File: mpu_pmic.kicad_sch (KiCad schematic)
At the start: 56 parts, among them J501 36103505, U501 STPMIC1DPQR

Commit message: Clean-up schematics
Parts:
- L501, L502, L503, L504: MPN (none) -> DFE252012P-1R0M=P2
- R504, R505, R506, R507, R508, R509: value 33 Ω -> 0 Ω
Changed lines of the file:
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@@
 			)
 		)
-		(property "MPN" ""
+		(property "MPN" "DFE252012P-1R0M=P2"
 			(at 208.28 129.54 90)
 			(effects
@@
 			)
 		)
-		(property "Value" "33 Ω"
+		(property "Value" "0 Ω"
 			(at 155.448 202.692 90)
 			(effects
@@
 			)
 		)
-		(property "MPN" ""
+		(property "MPN" "DFE252012P-1R0M=P2"
 			(at 208.28 137.16 90)
 			(effects
@@
 			)
 		)
-		(property "Value" "33 Ω"
+		(property "Value" "0 Ω"
 			(at 155.448 195.072 90)
 			(effects
@@
 			)
 		)
-		(property "Value" "33 Ω"
+		(property "Value" "0 Ω"
 			(at 155.448 200.152 90)
 			(effects
@@
 			)
 		)
-		(property "Value" "33 Ω"
+		(property "Value" "0 Ω"
 			(at 155.448 197.612 90)
 			(effects
@@
 			)
 		)
-		(property "Value" "33 Ω"
+		(property "Value" "0 Ω"
 			(at 155.448 192.532 90)
 			(effects
@@
 			)
 		)
-		(property "MPN" ""
+		(property "MPN" "DFE252012P-1R0M=P2"
 			(at 208.28 114.3 90)
 			(effects
@@
 			)
 		)
-		(property "MPN" ""
+		(property "MPN" "DFE252012P-1R0M=P2"
 			(at 208.28 121.92 90)
 			(effects
@@
 			)
 		)
-		(property "Value" "33 Ω"
+		(property "Value" "0 Ω"
 			(at 203.2 191.516 90)
 			(effects

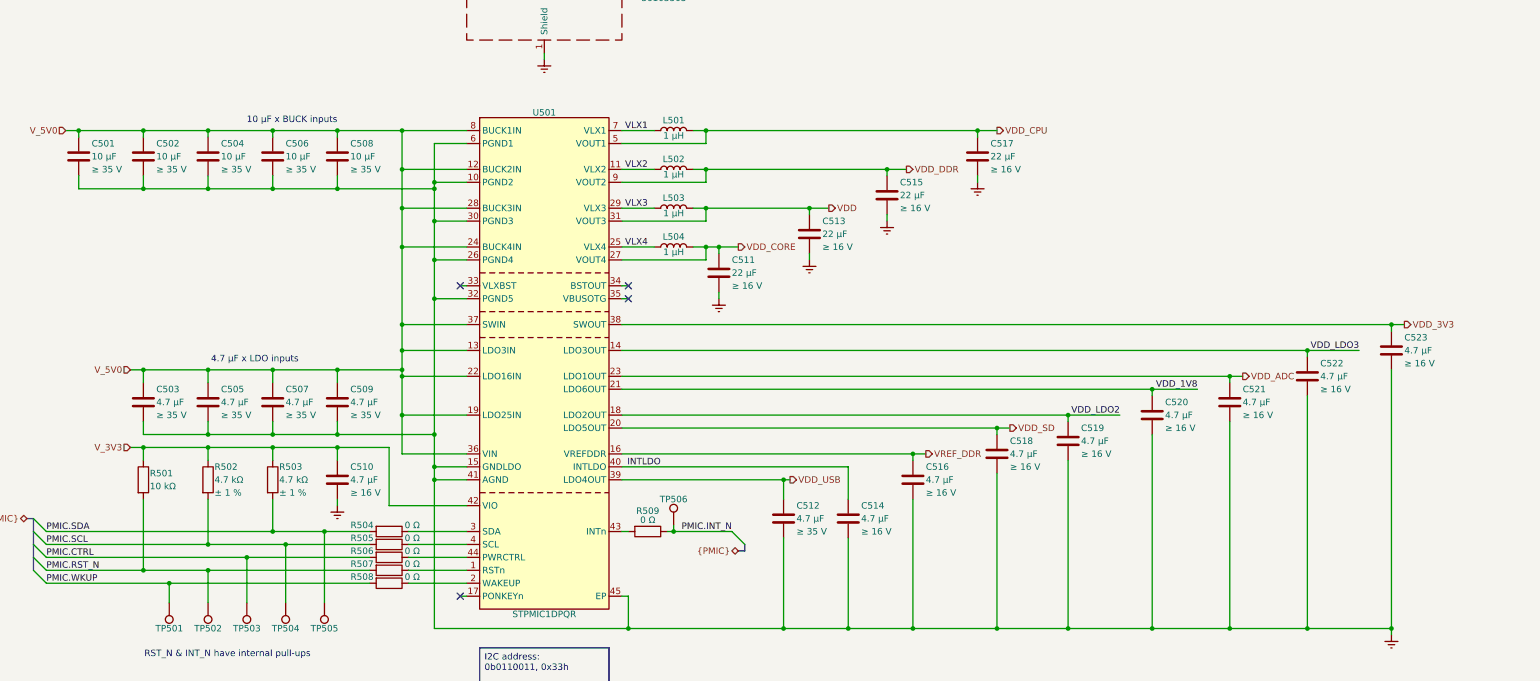
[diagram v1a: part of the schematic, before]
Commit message: Add additional info to passives
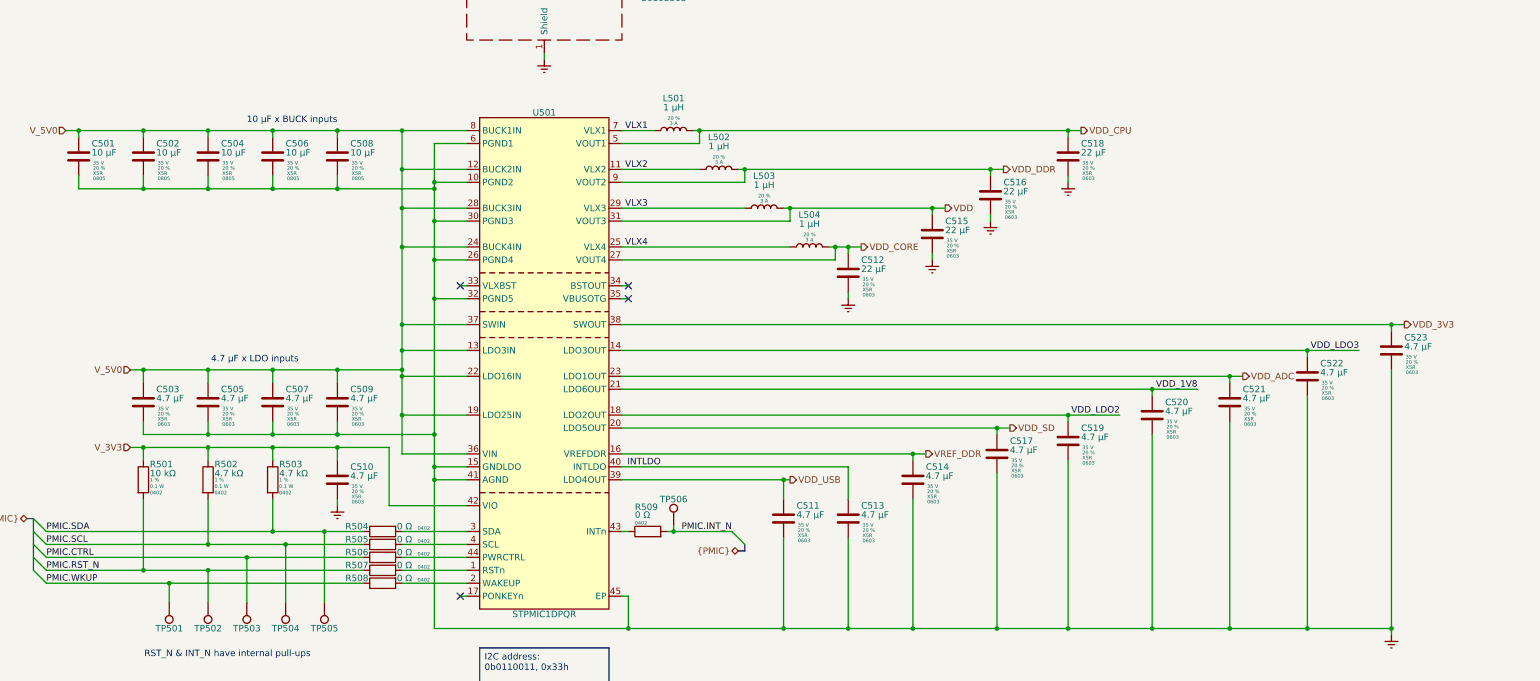
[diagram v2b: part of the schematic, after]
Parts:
- C501, C502, C504, C506, C508: footprint Capacitor_SMD:C_0603_1608Metric -> (none); MPN GRM188R6YA106MA73D -> (none); Manufacturer Murata Electronics -> (none); Size (none) -> 0805; Temperature coefficient (none) -> X5R; Tolerance (none) -> 20 %; Voltage rating ≥ 35 V -> 35 V
- C503, C505, C507, C509: footprint Capacitor_SMD:C_0603_1608Metric -> (none); MPN GRM188R6YA475KE15D -> (none); Manufacturer Murata Electronics -> (none); Size (none) -> 0603; Temperature coefficient (none) -> X5R; Tolerance (none) -> 20 %; Voltage rating ≥ 35 V -> 35 V
- C510, C514, C519, C520, C521, C522, C523: footprint Capacitor_SMD:C_0603_1608Metric -> (none); MPN GRM188R6YA475KE15D -> (none); Manufacturer Murata Electronics -> (none); Size (none) -> 0603; Temperature coefficient (none) -> X5R; Tolerance (none) -> 20 %; Voltage rating ≥ 16 V -> 35 V
- C511, C513, C517: value 22 µF -> 4.7 µF; footprint Capacitor_SMD:C_0603_1608Metric -> (none); MPN GRM188R6YA106MA73D -> (none); Manufacturer Murata Electronics -> (none); Size (none) -> 0603; Temperature coefficient (none) -> X5R; Tolerance (none) -> 20 %; Voltage rating ≥ 16 V -> 35 V
- C512: value 4.7 µF -> 22 µF; footprint Capacitor_SMD:C_0603_1608Metric -> (none); MPN GRM188R6YA475KE15D -> (none); Manufacturer Murata Electronics -> (none); Size (none) -> 0603; Temperature coefficient (none) -> X5R; Tolerance (none) -> 20 %; Voltage rating ≥ 35 V -> 35 V
- C515: footprint Capacitor_SMD:C_0603_1608Metric -> (none); MPN GRM188R6YA106MA73D -> (none); Manufacturer Murata Electronics -> (none); Size (none) -> 0603; Temperature coefficient (none) -> X5R; Tolerance (none) -> 20 %; Voltage rating ≥ 16 V -> 35 V
- C516, C518: value 4.7 µF -> 22 µF; footprint Capacitor_SMD:C_0603_1608Metric -> (none); MPN GRM188R6YA475KE15D -> (none); Manufacturer Murata Electronics -> (none); Size (none) -> 0603; Temperature coefficient (none) -> X5R; Tolerance (none) -> 20 %; Voltage rating ≥ 16 V -> 35 V
- L501, L502, L503, L504: footprint (none) -> Inductor_SMD:L_1008_2520Metric; Current rating (none) -> 3 A; Digi-Key Part Number (none) -> 490-10647-1-ND; Manufacturer (none) -> Murata Electronics; Tolerance (none) -> 20 %
- R501: MPN 560112110020 -> (none); Manufacturer Würth Elektronik -> (none); Power rating (none) -> 0.1 W; Size (none) -> 0402; Tolerance (none) -> 1 %
- R502, R503: Power rating (none) -> 0.1 W; Size (none) -> 0402; Tolerance ± 1 % -> 1 %
- R504, R505, R506, R507, R508, R509: footprint perfect_footprints:R_0402_1005Metric -> (none); MPN 560112110020 -> (none); Manufacturer Würth Elektronik -> (none); Size (none) -> 0402
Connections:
- net INTLDO: now also C513.1; no longer C514.1
- net PMIC.CTRL: now also R506.1; no longer R506.2
- net PMIC.INT_N: now also R509.2; no longer R509.1
- net PMIC.RST_N: now also R507.1; no longer R507.2
- net PMIC.SCL: now also R505.1; no longer R505.2
- net PMIC.SDA: now also R504.1; no longer R504.2
- net PMIC.WKUP: now also R508.1; no longer R508.2
- net VDD: now also C515.1; no longer C513.1
- net VDD_CORE: now also C512.1; no longer C511.1
- net VDD_CPU: now also C518.1; no longer C517.1
- net VDD_DDR: now also C516.1; no longer C515.1
- net VDD_SD: now also C517.1; no longer C518.1
- net VDD_USB: now also C511.1; no longer C512.1
- net VREF_DDR: now also C514.1; no longer C516.1
- net at U501.1 (RSTn): now also R507.2; no longer R507.1
- net at U501.2 (WAKEUP): now also R508.2; no longer R508.1
- net at U501.3 (SDA): now also R504.2; no longer R504.1
- net at U501.4 (SCL): now also R505.2; no longer R505.1
- net at U501.43 (INTn): now also R509.1; no longer R509.2
- net at U501.44 (PWRCTRL): now also R506.2; no longer R506.1

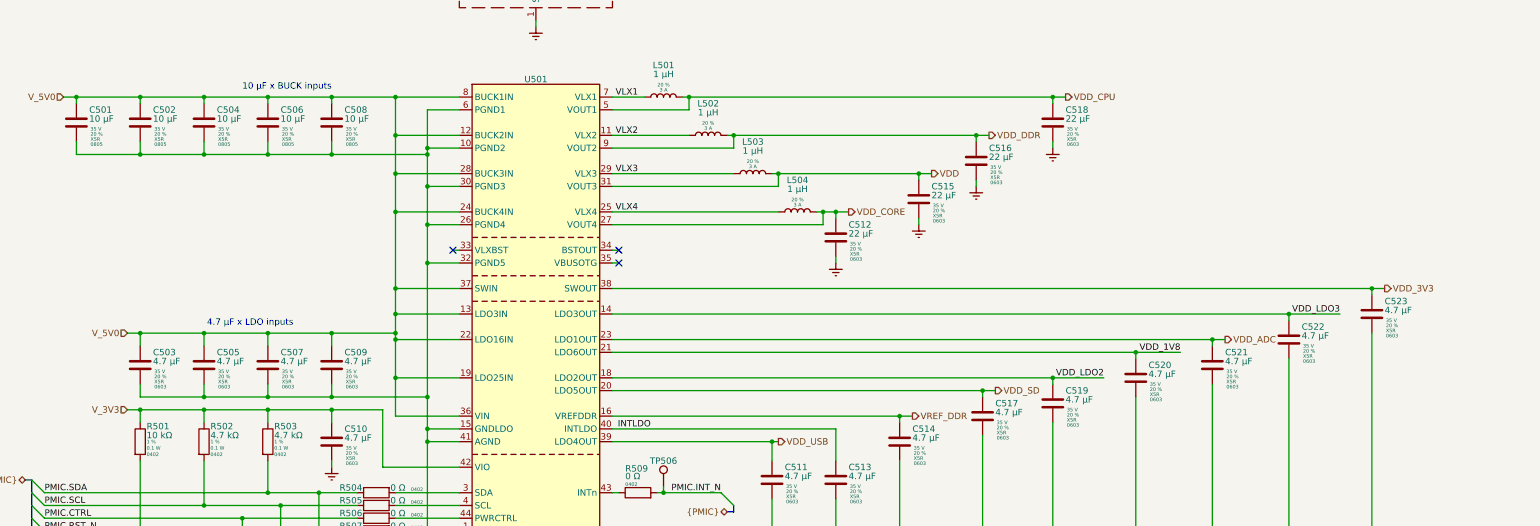
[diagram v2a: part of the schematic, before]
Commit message: Update capacitor BOM
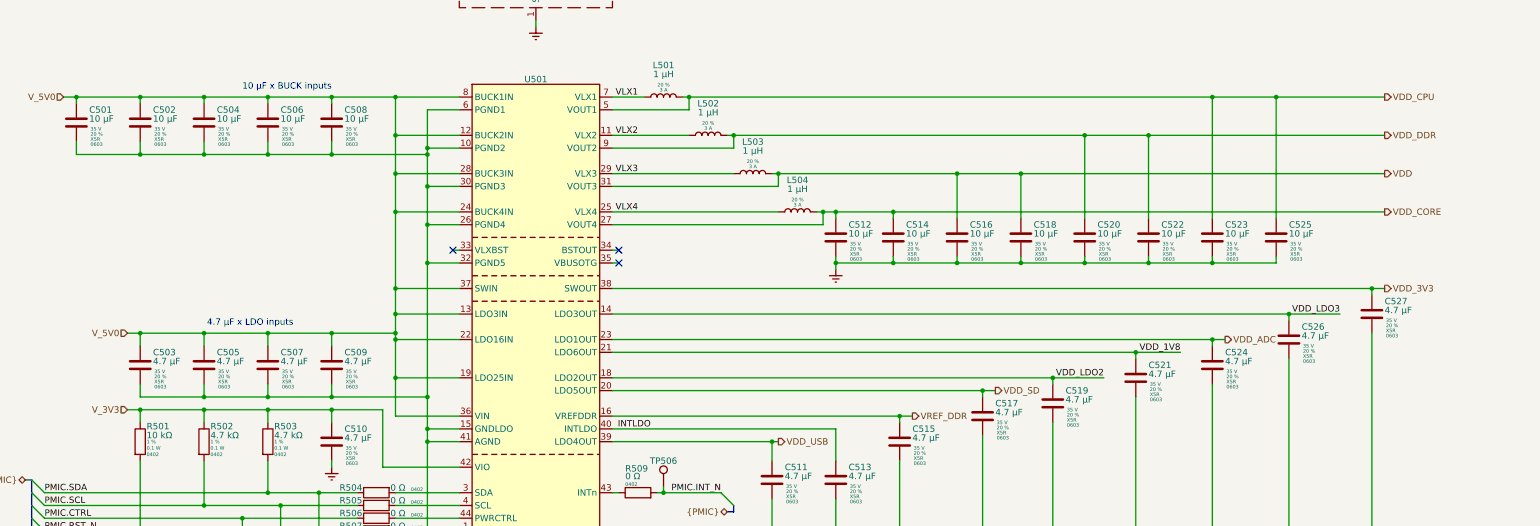
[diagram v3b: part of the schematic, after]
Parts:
- removed C515: 22 µF, symbol Device:C
- added C514, C520, C522, C523, C525: 10 µF, Capacitor_SMD:C_0603_1608Metric, symbol Device:C
- C501, C502, C504, C506, C508: footprint (none) -> Capacitor_SMD:C_0603_1608Metric; Digi-Key Part Number (none) -> 490-13248-1-ND; MPN (none) -> GRM188R6YA106MA73D; Manufacturer (none) -> Murata Electronics; Size 0805 -> 0603
- C503, C505, C507, C509, C510, C511, C513, C517, C519: footprint (none) -> Capacitor_SMD:C_0603_1608Metric; Digi-Key Part Number (none) -> 490-7205-1-ND; MPN (none) -> GRM188R6YA475KE15D; Manufacturer (none) -> Murata Electronics
- C512, C516, C518: value 22 µF -> 10 µF; footprint (none) -> Capacitor_SMD:C_0603_1608Metric; Digi-Key Part Number (none) -> 490-13248-1-ND; MPN (none) -> GRM188R6YA106MA73D; Manufacturer (none) -> Murata Electronics
- C515: renamed from C514; footprint (none) -> Capacitor_SMD:C_0603_1608Metric; Digi-Key Part Number (none) -> 490-7205-1-ND; MPN (none) -> GRM188R6YA475KE15D; Manufacturer (none) -> Murata Electronics
- C521: renamed from C520; footprint (none) -> Capacitor_SMD:C_0603_1608Metric; Digi-Key Part Number (none) -> 490-7205-1-ND; MPN (none) -> GRM188R6YA475KE15D; Manufacturer (none) -> Murata Electronics
- C524: renamed from C521; footprint (none) -> Capacitor_SMD:C_0603_1608Metric; Digi-Key Part Number (none) -> 490-7205-1-ND; MPN (none) -> GRM188R6YA475KE15D; Manufacturer (none) -> Murata Electronics
- C526: renamed from C522; footprint (none) -> Capacitor_SMD:C_0603_1608Metric; Digi-Key Part Number (none) -> 490-7205-1-ND; MPN (none) -> GRM188R6YA475KE15D; Manufacturer (none) -> Murata Electronics
- C527: renamed from C523; footprint (none) -> Capacitor_SMD:C_0603_1608Metric; Digi-Key Part Number (none) -> 490-7205-1-ND; MPN (none) -> GRM188R6YA475KE15D; Manufacturer (none) -> Murata Electronics
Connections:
- net GND: now also C514.2, C520.2, C522.2, C523.2, C525.2
- net VDD: now also C516.1, C518.1
- net VDD_CORE: now also C514.1
- net VDD_CPU: now also C523.1, C525.1; no longer C518.1
- net VDD_DDR: now also C520.1, C522.1; no longer C516.1
